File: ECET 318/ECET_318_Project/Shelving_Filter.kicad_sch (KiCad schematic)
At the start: 27 parts, among them U2 TL084, U3 TL081

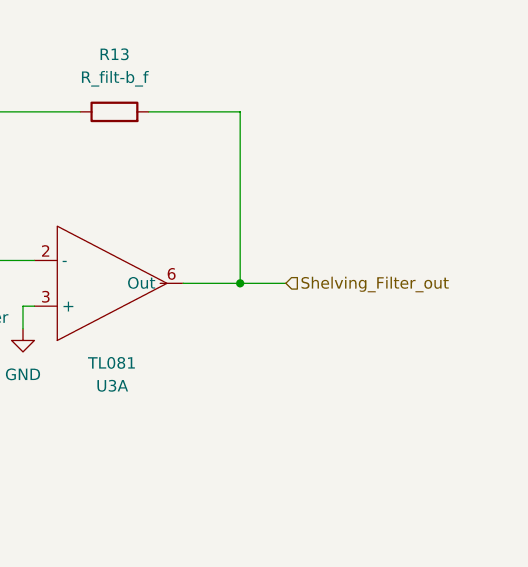
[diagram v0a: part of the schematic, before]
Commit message: Mostly finished Layout and change U5 to TL084
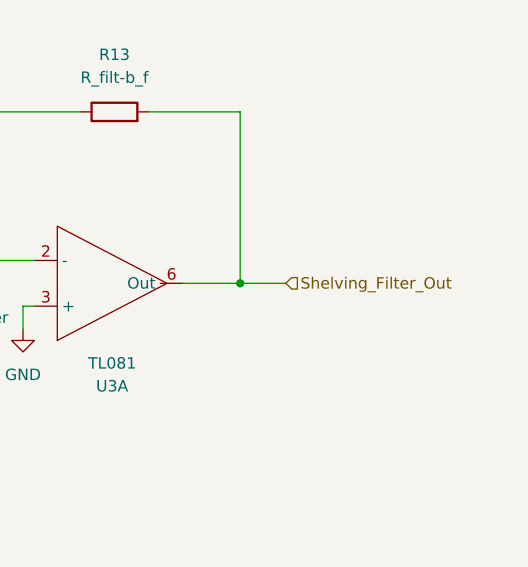
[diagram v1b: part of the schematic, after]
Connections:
- net Shelving_Filter_out renamed Shelving_Filter_Out

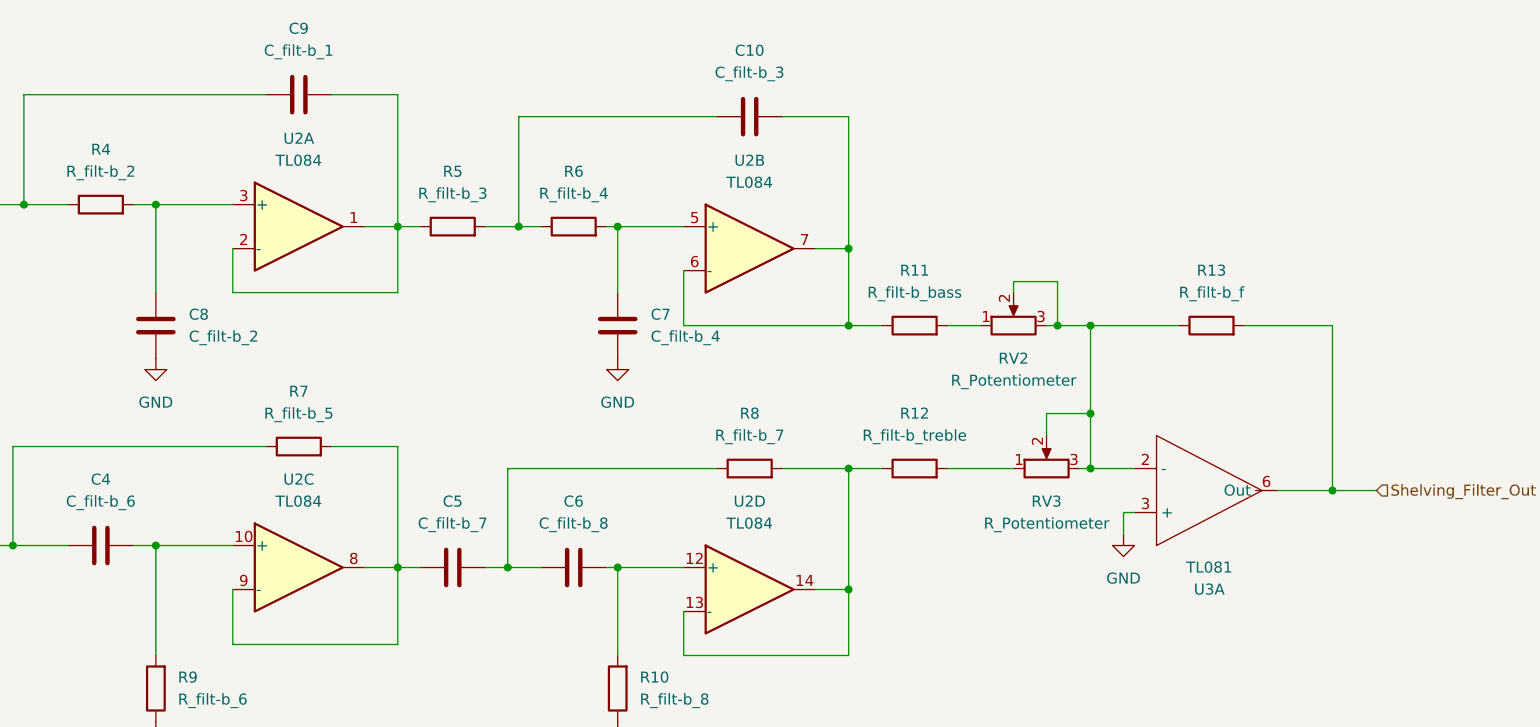
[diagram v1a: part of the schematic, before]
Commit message: Added Breadboard Space and Test Points
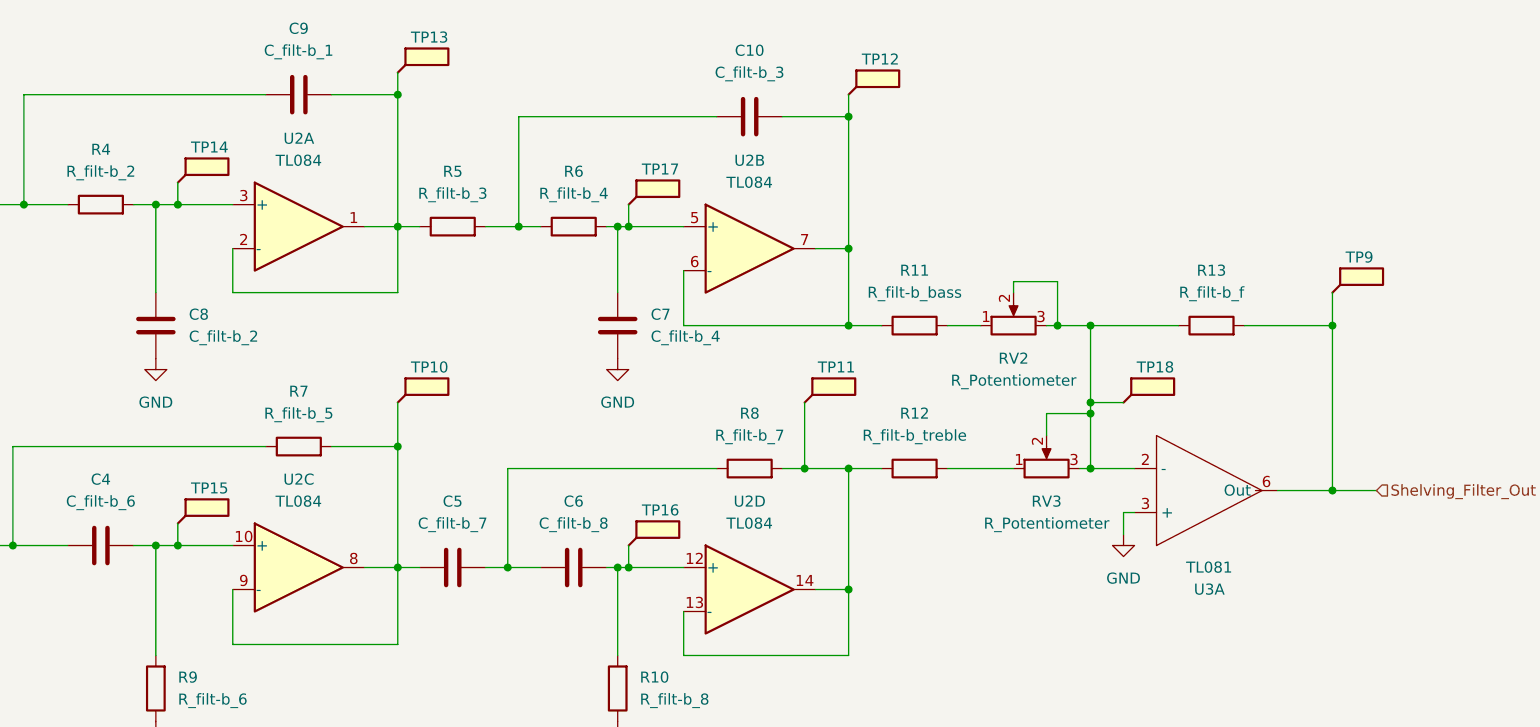
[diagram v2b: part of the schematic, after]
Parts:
- added TP10, TP11, TP12, TP13, TP14, TP15, TP16, TP17, TP18, TP9: TestPoint_Flag, TestPoint:TestPoint_Pad_D1.5mm, symbol Connector:TestPoint_Flag
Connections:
- net Shelving_Filter_Out: now also TP9.1
- net at C6.2, R10.2, U2.12 (+): now also TP16.1
- net at C7.2, R6.2, U2.5 (+): now also TP17.1
- net at R12.1, R8.2, U2.13 (-)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: now also TP11.1
- net at C9.1, R5.1, U2.1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: now also TP13.1
- net at C4.2, R9.2, U2.10 (+): now also TP15.1
- net at R13.1, RV2.2, RV2.3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: now also TP18.1
- net at C5.1, R7.2, U2.8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: now also TP10.1
- net at C8.2, R4.2, U2.3 (+): now also TP14.1
- net at C10.1, R11.1, U2.6 (-)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: now also TP12.1
